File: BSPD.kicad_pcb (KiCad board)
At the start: 2 copper layers, 77 x 54 mm, 85 parts, among them J1 Conn_01x03_Socket, J2 Conn_01x03_Socket, J3 Conn_01x02_Socket, J4 Conn_01x02_Socket, K1 Relay_SPST-NO, Q1 2N7002, Q2 2N7002, U1 74LVC1G11, U2 TPS7B88-Q1, U3 74LVC1G332, U4 LTC6994xS6-1, U5 LTC6994xS6-1, U6 74LVC1G332, U7 LM393, U8 LM393

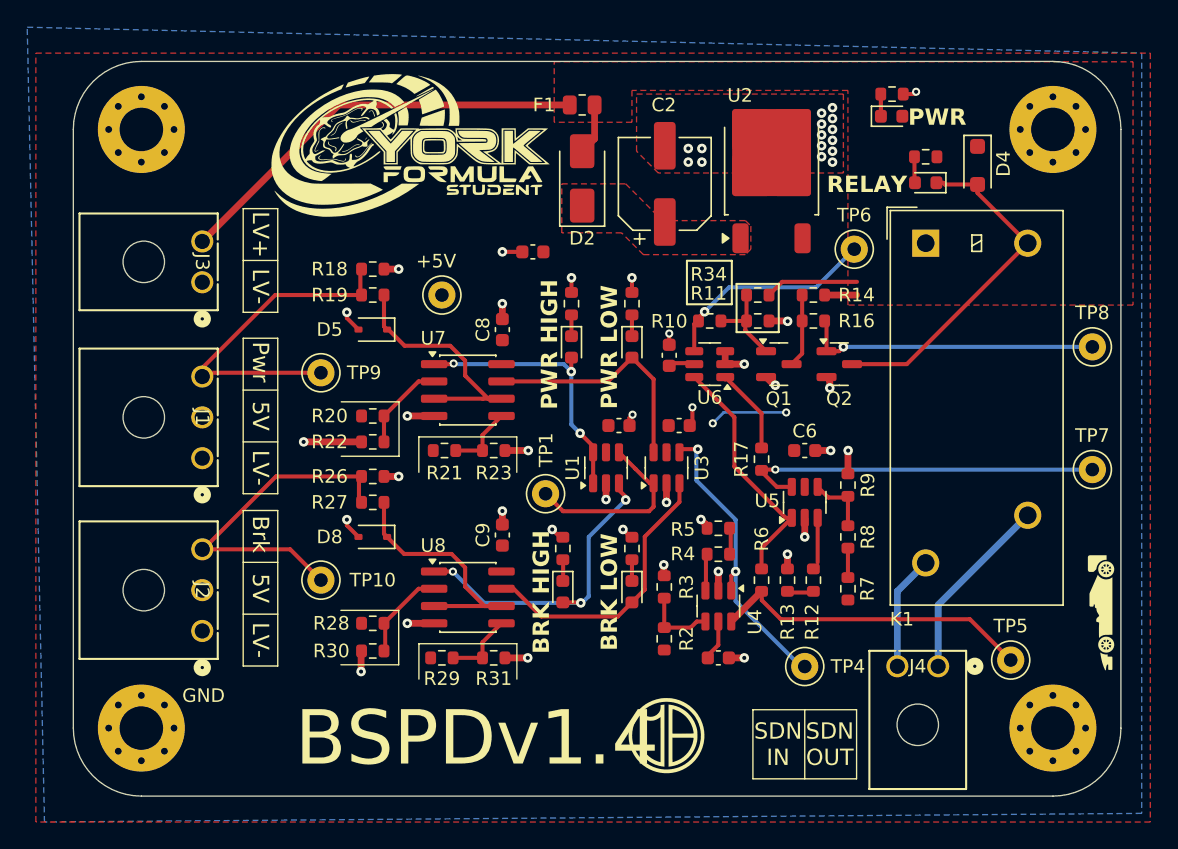
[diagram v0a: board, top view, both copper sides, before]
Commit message: Updated connector colours
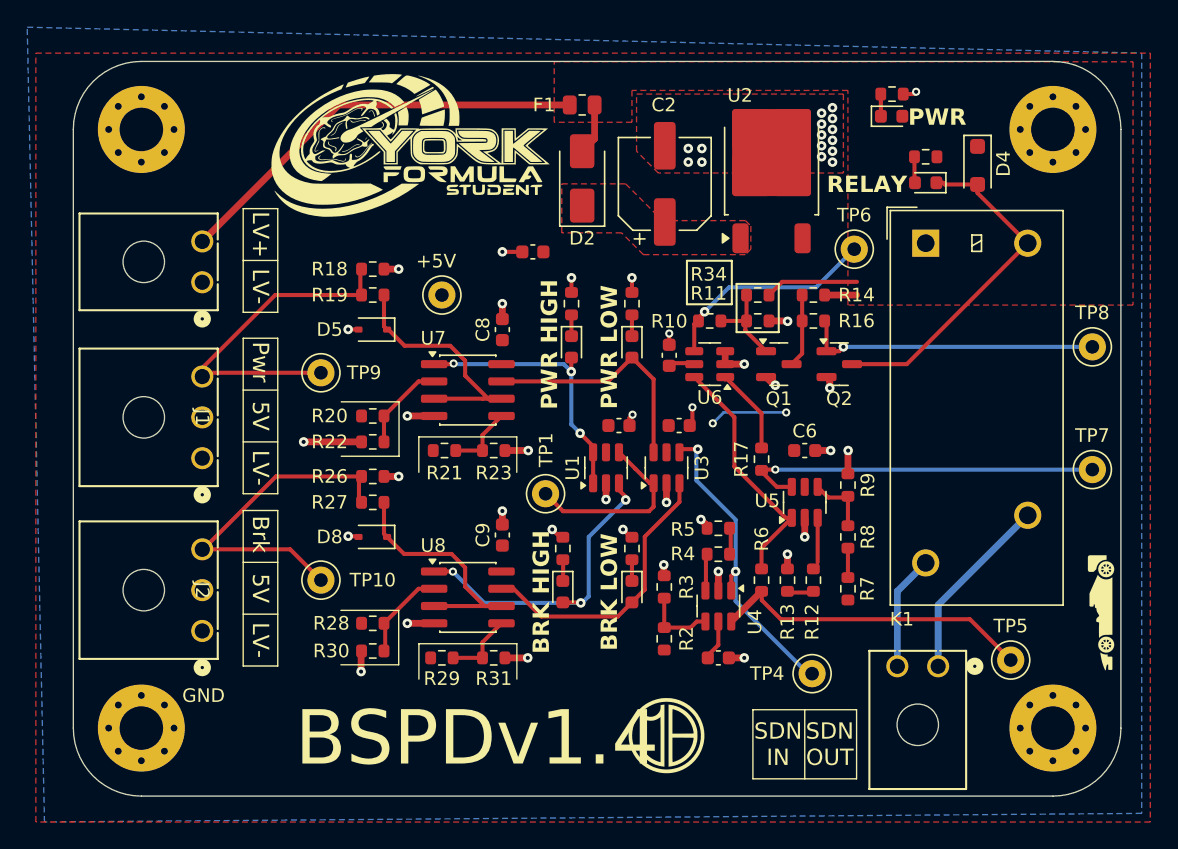
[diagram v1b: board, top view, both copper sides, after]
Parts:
- moved TP4 0.75 mm to (112.3, 118.0)
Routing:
- net GND: track 46.8 -> 45.1 mm
- net Net-(U4-IN): track 22.1 -> 23.2 mm
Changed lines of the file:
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@@
 			(unlocked yes)
 			(layer "F.SilkS")
+			(hide yes)
 			(effects
 				(font
@@
 		)
 		(embedded_fonts no)
-		(model "${KIPRJMOD}/kicad-library/models/MolexMicrofitPlus1x2.stp"
+		(model "${KIPRJMOD}/kicad-library/models/MolexMicrofitPlus1x2-Red.stp"
 			(offset
 				(xyz -1.5 -4 0)
@@
 	(footprint "TestPoint:TestPoint_Keystone_5000-5004_Miniature"
 		(layer "F.Cu")
-		(at 111.76 117.475)
+		(at 112.3 118)
 		(descr "Keystone THM Miniature Test Point 5000-5004, http://www.keyelco.com/product-pdf.cfm?p=1309")
 		(tags "Through Hole Mount Test Points")
 		(property "Reference" "TP4"
-			(at 3.175 0 0)
+			(at -3.3 0 0)
 			(layer "F.SilkS")
 			(effects
@@
 			(unlocked yes)
 			(layer "F.SilkS")
+			(hide yes)
 			(effects
 				(font
@@
 		)
 		(embedded_fonts no)
-		(model "${KIPRJMOD}/kicad-library/models/MolexMicrofitPlus1x2.stp"
+		(model "${KIPRJMOD}/kicad-library/models/MolexMicrofitPlus1x2-Blue.stp"
 			(offset
 				(xyz -1.5 -4 0)
@@
 	)
 	(segment
-		(start 78.105 106.68)
-		(end 78.105 107.095)
-		(width 0.3)
-		(layer "F.Cu")
-		(net 1)
-	)
-	(segment
 		(start 89.54 87)
 		(end 91 87)
@@
 	)
 	(segment
-		(start 78.105 107.095)
-		(end 78.96 107.95)
-		(width 0.3)
+		(start 97.155 104.0075)
+		(end 97.155 105.2)
+		(width 0.5)
 		(layer "F.Cu")
 		(net 1)
 	)
 	(segment
-		(start 97.155 104.0075)
-		(end 97.155 105.2)
-		(width 0.5)
+		(start 78.91 107.9)
+		(end 78.96 107.95)
+		(width 0.3)
 		(layer "F.Cu")
 		(net 1)
@@
 	)
 	(segment
-		(start 78.105 91.855)
-		(end 78.96 92.71)
-		(width 0.3)
+		(start 104.4975 107.0375)
+		(end 104.4975 107.315)
+		(width 0.5)
 		(layer "F.Cu")
 		(net 1)
 	)
 	(segment
-		(start 104.4975 107.0375)
-		(end 104.4975 107.315)
-		(width 0.5)
+		(start 78.95 92.7)
+		(end 78.96 92.71)
+		(width 0.3)
 		(layer "F.Cu")
 		(net 1)
@@
 	)
 	(segment
+		(start 78.2 107.9)
+		(end 78.91 107.9)
+		(width 0.3)
+		(layer "F.Cu")
+		(net 1)
+	)
+	(segment
 		(start 113.6 96.4375)
 		(end 113.3625 96.2)
@@
 	)
 	(segment
-		(start 78.105 91.44)
-		(end 78.105 91.855)
-		(width 0.3)
-		(layer "F.Cu")
-		(net 1)
-	)
-	(segment
 		(start 119 75.4)
 		(end 119.775 75.4)
@@
 		(net 1)
 	)
+	(segment
+		(start 78.2 92.7)
+		(end 78.95 92.7)
+		(width 0.3)
+		(layer "F.Cu")
+		(net 1)
+	)
 	(via
 		(at 97.155 105.2)
@@
 	)
 	(via
-		(at 78.105 91.44)
+		(at 78.2 92.7)
 		(size 0.7)
 		(drill 0.3)
@@
 	)
 	(via
-		(at 78.105 106.68)
+		(at 78.2 107.9)
 		(size 0.7)
 		(drill 0.3)
@@
 	)
 	(segment
+		(start 106.68 112.68)
+		(end 106.68 110.49)
+		(width 0.3)
+		(layer "B.Cu")
+		(net 27)
+	)
+	(segment
 		(start 103.8 101.6)
 		(end 103.8 103.8)
@@
 	)
 	(segment
-		(start 106.68 112.68)
-		(end 106.68 110.49)
+		(start 112.3 118)
+		(end 112 118)
 		(width 0.3)
 		(layer "B.Cu")
@@
 	)
 	(segment
-		(start 103.9 101.5)
-		(end 103.8 101.6)
+		(start 112 118)
+		(end 106.68 112.68)
 		(width 0.3)
 		(layer "B.Cu")
@@
 	)
 	(segment
-		(start 111.4 117.4)
-		(end 106.68 112.68)
+		(start 103.9 101.5)
+		(end 103.8 101.6)
 		(width 0.3)
 		(layer "B.Cu")
